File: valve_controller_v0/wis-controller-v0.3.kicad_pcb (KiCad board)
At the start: 2 copper layers, 78 x 110 mm, 68 parts, among them J1 18650 Socket, J11 Solenoid_connector, J3 USB_C_Receptacle_USB2.0, J5 SWD, J6 JST-2PH, Q1 DMG3415UQ-7, SW1 RESET, SW3 SW_DIP_x02, SW4 BOOT, U1 RAK3172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

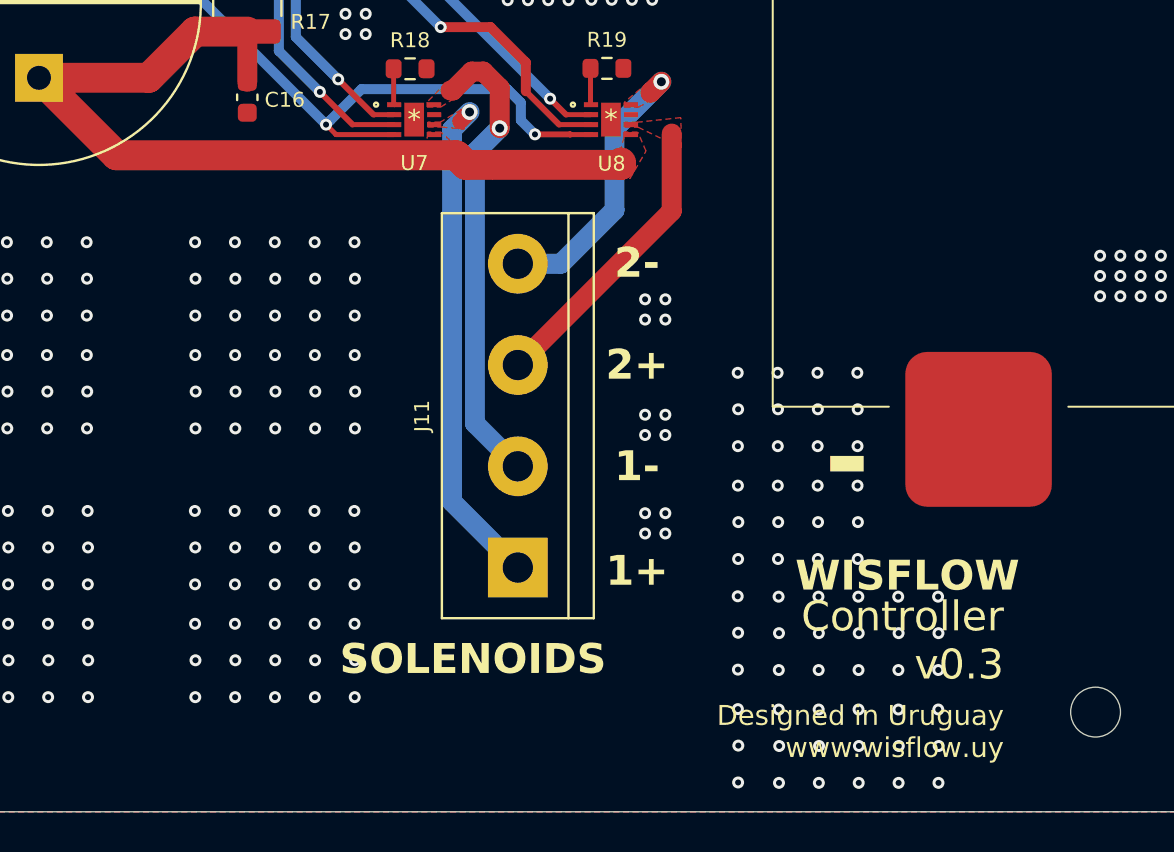
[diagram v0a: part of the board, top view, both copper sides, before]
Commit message: Solenoid terminal block relocated
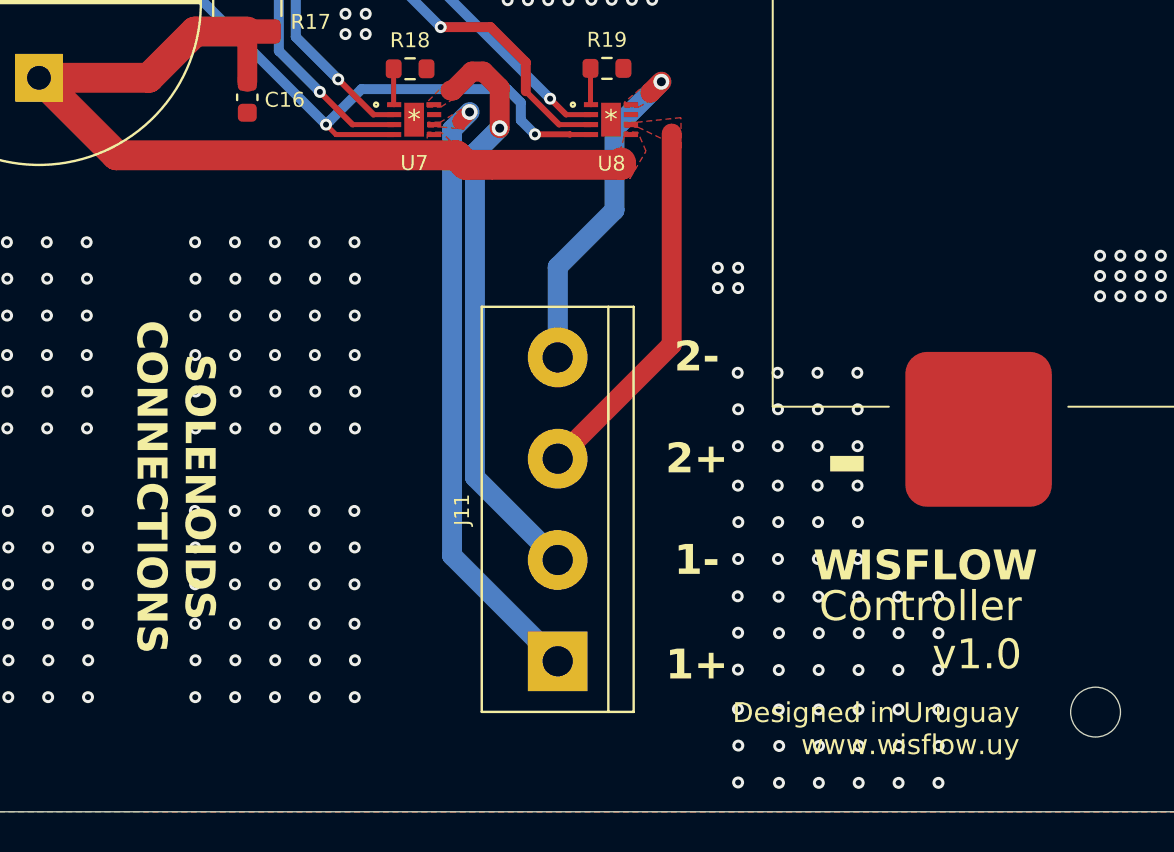
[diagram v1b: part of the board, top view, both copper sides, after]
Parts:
- moved J11 5.11 mm to (146.0, 122.5)
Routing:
- net Net-(J11-Pin_2): track 23.6 -> 29.1 mm
- net Net-(J11-Pin_1): track 25.2 -> 30.8 mm
- net Net-(J11-Pin_3): track 14.8 -> 18.7 mm
- net Net-(J11-Pin_4): track 14.2 -> 16.8 mm
- net GND: vias 665 -> 657
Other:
- board text added: "Controller v1.0"
- board text added: "SOLENOIDS CONNECTIONS"
- board text removed: "Controller v0.3"
- board text removed: "SOLENOIDS"

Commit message: Updated v0.3 for fabrication
- Removed unnecesary via in U11 pad2
- Solved courtyard overlaping of J3-D1, J3-R2, U1-C4 and U1-C1
- Removed silkscreen for R6 and U3
- Generated manufacturing files (production folder)
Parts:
- moved D1 0.06 mm to (101.8, 36.5)
- moved R2 0.05 mm to (105.2, 36.5)
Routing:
- net unconnected-(U11-Pad2): track 1.23 -> 0.00 mm, vias 1 -> 0
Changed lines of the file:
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@@
 	(footprint "Capacitor_SMD:C_0603_1608Metric"
 		(layer "F.Cu")
-		(at 125.412 45.4102 180)
+		(at 125.3866 45.4102 180)
 		(descr "Capacitor SMD 0603 (1608 Metric), square (rectangular) end terminal, IPC_7351 nominal, (Body size source: IPC-SM-782 page 76, https://www.pcb-3d.com/wordpress/wp-content/uploads/ipc-sm-782a_amendment_1_and_2.pdf), generated with kicad-footprint-generator")
 		(tags "capacitor")
@@
 	(footprint "Capacitor_SMD:C_0603_1608Metric"
 		(layer "F.Cu")
-		(at 126.174 47.6838 -90)
+		(at 126.1486 47.6838 -90)
 		(descr "Capacitor SMD 0603 (1608 Metric), square (rectangular) end terminal, IPC_7351 nominal, (Body size source: IPC-SM-782 page 76, https://www.pcb-3d.com/wordpress/wp-content/uploads/ipc-sm-782a_amendment_1_and_2.pdf), generated with kicad-footprint-generator")
 		(tags "capacitor")
@@
 	(footprint "Resistor_SMD:R_0603_1608Metric"
 		(layer "F.Cu")
-		(at 105.16 36.55 180)
+		(at 105.16 36.4992 180)
 		(descr "Resistor SMD 0603 (1608 Metric), square (rectangular) end terminal, IPC_7351 nominal, (Body size source: IPC-SM-782 page 72, https://www.pcb-3d.com/wordpress/wp-content/uploads/ipc-sm-782a_amendment_1_and_2.pdf), generated with kicad-footprint-generator")
 		(tags "resistor")
@@
 			(at 0 -2.4 90)
 			(layer "F.SilkS")
+			(hide yes)
 			(effects
 				(font
@@
 	(footprint "Capacitor_SMD:C_0603_1608Metric"
 		(layer "F.Cu")
-		(at 124.65 47.6838 -90)
+		(at 124.6246 47.6838 -90)
 		(descr "Capacitor SMD 0603 (1608 Metric), square (rectangular) end terminal, IPC_7351 nominal, (Body size source: IPC-SM-782 page 76, https://www.pcb-3d.com/wordpress/wp-content/uploads/ipc-sm-782a_amendment_1_and_2.pdf), generated with kicad-footprint-generator")
 		(tags "capacitor")
@@
 			(at 0 -1.43 90)
 			(layer "F.SilkS")
+			(hide yes)
 			(effects
 				(font
@@
 	(footprint "LED_SMD:LED_0603_1608Metric"
 		(layer "F.Cu")
-		(at 101.8315 36.5475)
+		(at 101.826014 36.48706)
 		(descr "LED SMD 0603 (1608 Metric), square (rectangular) end terminal, IPC_7351 nominal, (Body size source: http://www.tortai-tech.com/upload/download/2011102023233369053.pdf), generated with kicad-footprint-generator")
 		(tags "LED")
@@
 		(layer "Edge.Cuts")
 	)
-	(gr_text "-"
-		(at 167.45 79.23 90)
+	(gr_text "Designed in Uruguay\nwww.wisflow.uy"
+		(at 169.19 125.84 0)
 		(layer "F.SilkS")
 		(effects
 			(font
-				(size 4 4)
-				(thickness 1)
-				(bold yes)
+				(size 1 1)
+				(thickness 0.18)
 			)
+			(justify right)
 		)
 	)
-	(gr_text "9V"
-		(at 113.59 77.55 0)
+	(gr_text "BOOT"
+		(at 102.18 28.14 0)
 		(layer "F.SilkS")
 		(effects
 			(font
-				(size 1.5 1.5)
-				(thickness 0.375)
+				(size 1 1)
+				(thickness 0.2)
 				(bold yes)
 			)
 		)
 	)
-	(gr_text "RESET"
-		(at 108.79 31.18 0)
+	(gr_text "ON/OFF"
+		(at 103.08 58.98 0)
 		(layer "F.SilkS")
 		(effects
@@
 		)
 	)
-	(gr_text "1+"
-		(at 153 122.62 0)
+	(gr_text "RESET"
+		(at 108.79 31.18 0)
 		(layer "F.SilkS")
 		(effects
 			(font
-				(size 1.5 1.5)
-				(thickness 0.375)
+				(size 1 1)
+				(thickness 0.2)
 				(bold yes)
 			)
 		)
 	)
-	(gr_text "2+"
-		(at 153 112.28 0)
+	(gr_text "Controller\nv1.0"
+		(at 169.3 120.9 0)
 		(layer "F.SilkS")
 		(effects
 			(font
 				(size 1.5 1.5)
-				(thickness 0.375)
-				(bold yes)
+				(thickness 0.2)
 			)
+			(justify right)
 		)
 	)
@@
 		)
 	)
-	(gr_text "2-"
-		(at 153 107.17 0)
+	(gr_text "14V"
+		(at 112.86 75.35 0)
 		(layer "F.SilkS")
 		(effects
@@
 		)
 	)
-	(gr_text "BATTERY"
-		(at 167.45 66.19 90)
+	(gr_text "9V"
+		(at 113.59 77.55 0)
 		(layer "F.SilkS")
 		(effects
 			(font
-				(size 3 3)
-				(thickness 0.5)
+				(size 1.5 1.5)
+				(thickness 0.375)
+				(bold yes)
 			)
 		)
 	)
-	(gr_text "14V"
-		(at 112.86 75.35 0)
+	(gr_text "VOLTAGE"
+		(at 119.77 72.54 0)
 		(layer "F.SilkS")
 		(effects
@@
 		)
 	)
-	(gr_text "SOLENOIDS\nCONNECTIONS"
-		(at 126.85 113.71 270)
+	(gr_text "2-"
+		(at 153 107.17 0)
 		(layer "F.SilkS")
 		(effects
@@
 		)
 	)
-	(gr_text "ON/OFF"
-		(at 103.08 58.98 0)
+	(gr_text "2+"
+		(at 153 112.28 0)
 		(layer "F.SilkS")
 		(effects
 			(font
-				(size 1 1)
-				(thickness 0.2)
+				(size 1.5 1.5)
+				(thickness 0.375)
 				(bold yes)
 			)
 		)
 	)
-	(gr_text "BOOT"
-		(at 102.18 28.14 0)
+	(gr_text "1-"
+		(at 153 117.37 0)
 		(layer "F.SilkS")
 		(effects
 			(font
-				(size 1 1)
-				(thickness 0.2)
+				(size 1.5 1.5)
+				(thickness 0.375)
 				(bold yes)
 			)
 		)
 	)
-	(gr_text "-"
-		(at 106.78 60.3 0)
+	(gr_text "1+"
+		(at 153 122.62 0)
 		(layer "F.SilkS")
 		(effects
 			(font
-				(size 2 2)
-				(thickness 0.5)
+				(size 1.5 1.5)
+				(thickness 0.375)
 				(bold yes)
 			)
 		)
 	)
-	(gr_text "Designed in Uruguay\nwww.wisflow.uy"
-		(at 169.19 125.84 0)
+	(gr_text "WISFLOW"
+		(at 164.46 117.65 0)
 		(layer "F.SilkS")
 		(effects
 			(font
-				(size 1 1)
-				(thickness 0.18)
+				(size 1.5 1.5)
+				(thickness 0.375)
+				(bold yes)
 			)
-			(justify right)
 		)
 	)
-	(gr_text "VOLTAGE"
-		(at 119.77 72.54 0)
+	(gr_text "SOLENOIDS\nCONNECTIONS"
+		(at 126.85 113.71 270)
 		(layer "F.SilkS")
 		(effects
@@
 		)
 	)
-	(gr_text "Controller\nv1.0"
-		(at 169.3 120.9 0)
+	(gr_text "-"
+		(at 106.78 60.3 0)
 		(layer "F.SilkS")
 		(effects
 			(font
-				(size 1.5 1.5)
-				(thickness 0.2)
+				(size 2 2)
+				(thickness 0.5)
+				(bold yes)
 			)
-			(justify right)
 		)
 	)
-	(gr_text "1-"
-		(at 153 117.37 0)
+	(gr_text "+"
+		(at 106.89 62.35 0)
 		(layer "F.SilkS")
 		(effects
 			(font
-				(size 1.5 1.5)
-				(thickness 0.375)
+				(size 2 2)
+				(thickness 0.5)
 				(bold yes)
 			)
 		)
 	)
-	(gr_text "+"
-		(at 167.45 54.31 0)
+	(gr_text "BATTERY"
+		(at 167.45 66.19 90)
 		(layer "F.SilkS")
 		(effects
 			(font
-				(size 4 4)
-				(thickness 1)
-				(bold yes)
+				(size 3 3)
+				(thickness 0.5)
 			)
 		)
@@
 	)
 	(gr_text "+"
-		(at 106.89 62.35 0)
+		(at 167.45 54.31 0)
 		(layer "F.SilkS")
 		(effects
 			(font
-				(size 2 2)
-				(thickness 0.5)
+				(size 4 4)
+				(thickness 1)
 				(bold yes)
 			)
 		)
 	)
-	(gr_text "WISFLOW"
-		(at 164.46 117.65 0)
+	(gr_text "-"
+		(at 167.45 79.23 90)
 		(layer "F.SilkS")
 		(effects
 			(font
-				(size 1.5 1.5)
-				(thickness 0.375)
+				(size 4 4)
+				(thickness 1)
 				(bold yes)
 			)
 		)
 	)
-	(gr_text "SWD"
-		(at 140.6266 42.159 270)
+	(gr_text "Rev 9.1"
+		(at 111.045 44.826 0)
 		(layer "B.SilkS")
 		(effects
 			(font
 				(size 0.8 0.8)
-				(thickness 0.15)
+				(thickness 0.1)
 			)
 			(justify mirror)
 		)
 	)
-	(gr_text "Rev 9.1"
-		(at 111.045 44.826 0)
+	(gr_text "SWD"
+		(at 140.6266 42.159 270)
 		(layer "B.SilkS")
 		(effects
 			(font
 				(size 0.8 0.8)
-				(thickness 0.1)
+				(thickness 0.15)
 			)
 			(justify mirror)
@@
 	)
 	(segment
-		(start 104.3325 36.5475)
-		(end 104.335 36.55)
+		(start 102.625654 36.4992)
+		(end 104.335 36.4992)
 		(width 0.2)
 		(layer "F.Cu")
@@
 	)
 	(segment
-		(start 102.619 36.5475)
-		(end 104.3325 36.5475)
+		(start 102.613514 36.48706)
+		(end 102.625654 36.4992)
 		(width 0.2)
 		(layer "F.Cu")
@@
 	)
 	(segment
+		(start 105.985 36.4992)
+		(end 108.2542 34.23)
+		(width 0.2)
+		(layer "F.Cu")
+		(net 40)
+	)
+	(segment
 		(start 126.746 38.989)
 		(end 127.007 39.25)
@@
 	)
 	(segment
-		(start 108.305 34.23)
+		(start 108.2542 34.23)
 		(end 118.18 34.23)
 		(width 0.2)
@@
 		(net 40)
 	)
-	(segment
-		(start 105.985 36.55)
-		(end 108.305 34.23)
-		(width 0.2)
-		(layer "F.Cu")
-		(net 40)
-	)
 	(via
 		(at 118.18 34.23)
@@
 	)
 	(segment
-		(start 105.25 57.23)
-		(end 104.03 57.23)
-		(width 0.25)
-		(layer "F.Cu")
-		(net 75)
-	)
-	(segment
-		(start 104.03 57.23)
-		(end 104.02 57.24)
-		(width 0.25)
-		(layer "F.Cu")
-		(net 75)
-	)
-	(via
-		(at 105.25 57.23)
-		(size 0.6)
-		(drill 0.3)
-		(layers "F.Cu" "B.Cu")
-		(net 75)
-	)
-	(segment

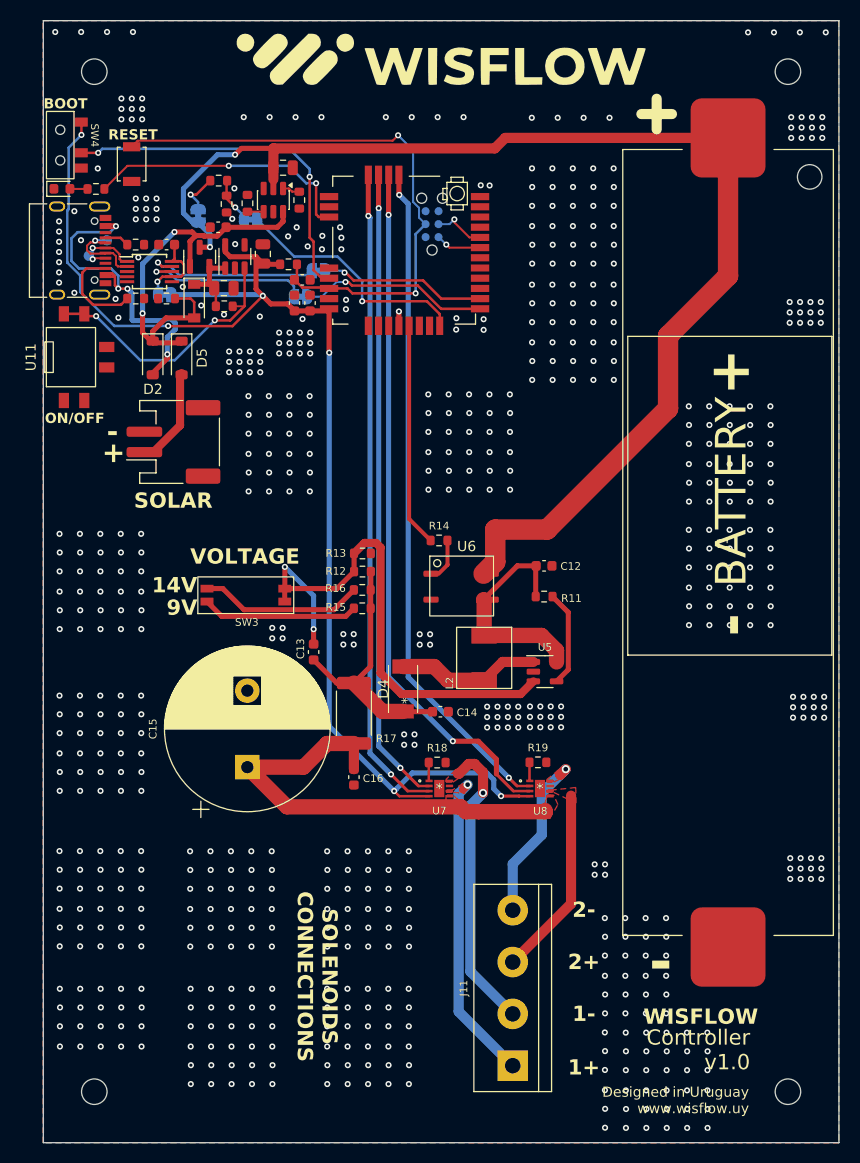
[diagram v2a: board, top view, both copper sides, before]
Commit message: Updated the 18650 battery holder
Changed the battery holder for the 18650 battery. Created new footprint and updated the PCB layout. Added cutouts for zip-ties
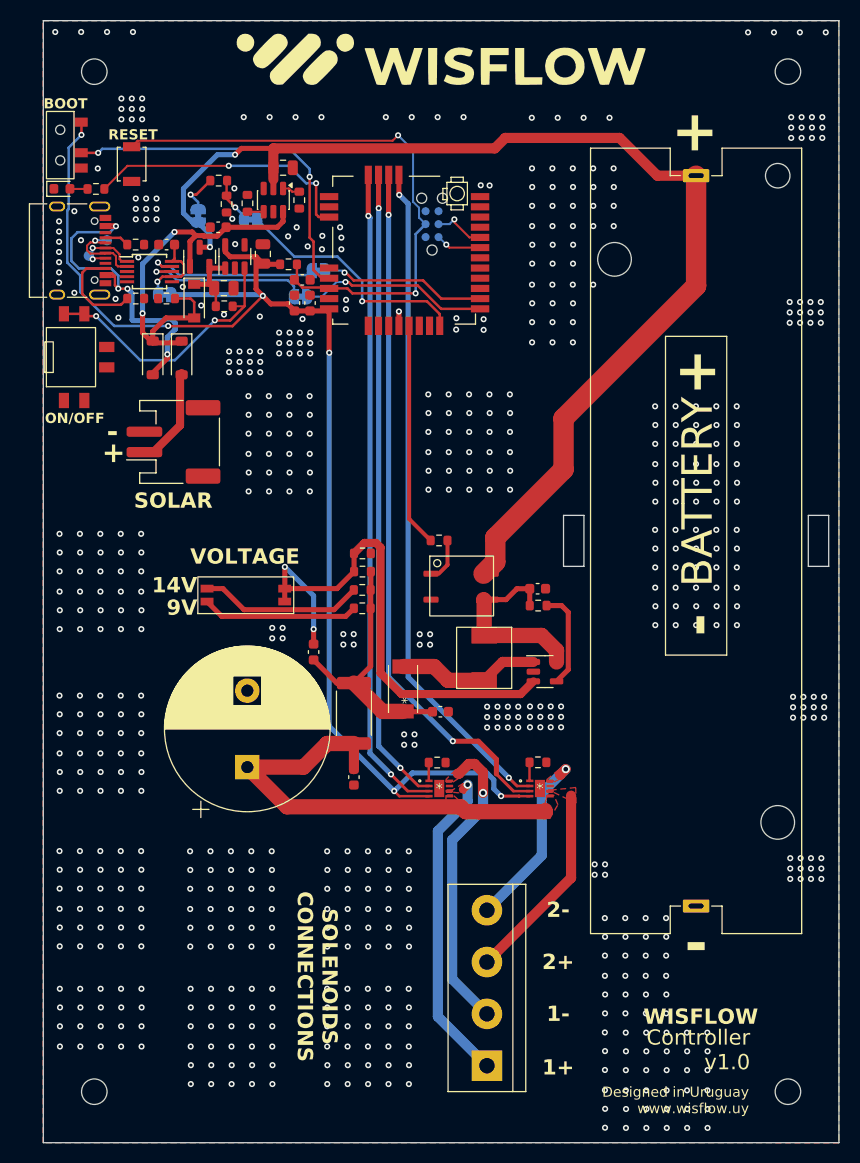
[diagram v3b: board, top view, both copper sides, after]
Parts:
- J1: footprint Wisflow:18650_SMD -> Wisflow:BatteryHolder_MPD_BK-18650-PC2
- moved J1 3.14 mm to (164.0, 71.0)
- moved J11 2.53 mm to (143.5, 122.5)
- moved C12 2.33 mm to (148.5, 75.7)
- moved R11 1.06 mm to (148.5, 77.3)
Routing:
- net +BATT: track 122.2 -> 112.7 mm
- net VIN: track 21.9 -> 19.0 mm
- net Net-(J11-Pin_4): track 16.8 -> 17.9 mm
- net Net-(J11-Pin_3): track 18.7 -> 19.7 mm
- net Net-(J11-Pin_1): track 30.8 -> 31.4 mm
- net GND: vias 657 -> 636
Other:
- outline, holes or cut-outs redrawn
